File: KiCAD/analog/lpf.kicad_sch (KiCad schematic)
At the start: 74 parts, among them J16 Screw_Terminal_01x02, J25 Screw_Terminal_01x02, J26 Screw_Terminal_01x02, J27 Screw_Terminal_01x02, J28 Filter In, K1 Relay_RSS-SR042P, K2 Relay_RSS-SR042P, K3 Relay_RSS-SR042P, K4 Relay_RSS-SR042P, Q1 2N7000, Q3 2N7000, Q8 2N7000, Q9 2N7000, U2 LM7171xIN

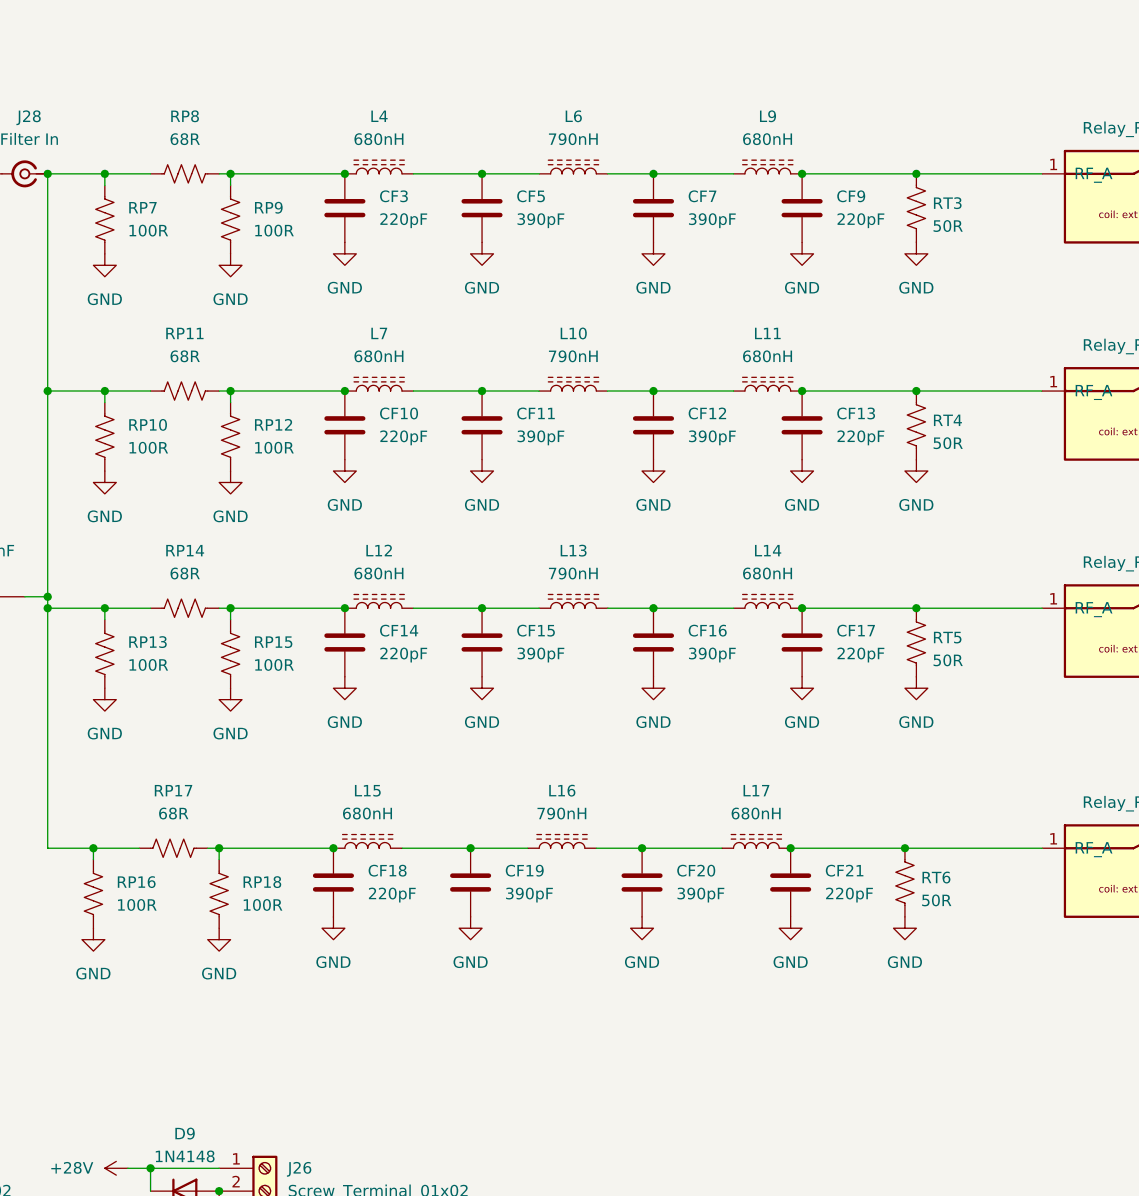
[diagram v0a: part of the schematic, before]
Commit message: KiCad revC: band-ID test points on each LPF input
Four test points added at the input node of each LPF (just after the
pi attenuator pad, at the junction with C1 shunt cap).  Reference
designators encode the band so that netlist/schematic consumers can
unambiguously identify which LPF cluster is for which band:

  TP20M  at 20 m LPF input
  TP17M  at 17 m LPF input
  TP15M  at 15 m LPF input
  TP10M  at 10 m LPF input

Dual-purpose: provides bench-probe access to the per-band LPF input
signal for debugging, and gives silkscreen labels on the PCB that make
the band assignment obvious at assembly time.

Co-Authored-By: Claude Opus 4.7 <noreply@anthropic.com>
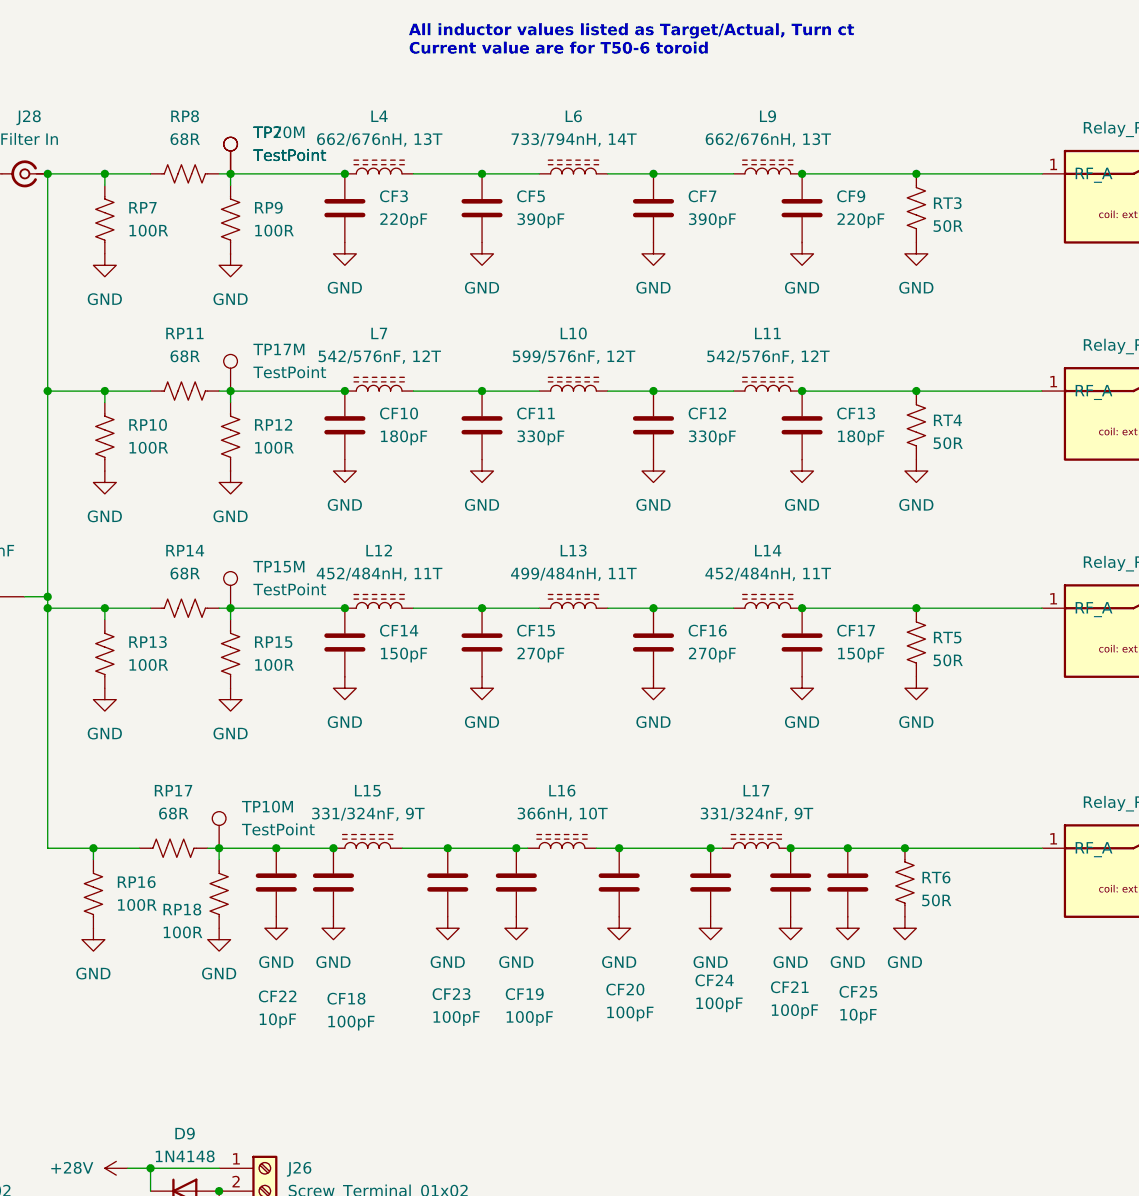
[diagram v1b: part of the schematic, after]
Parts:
- added CF22, CF25: 10pF, Capacitor_THT:C_Disc_D6.0mm_W2.5mm_P5.00mm, symbol Device:C
- added CF23, CF24: 100pF, Capacitor_THT:C_Disc_D6.0mm_W2.5mm_P5.00mm, symbol Device:C
- added TP10M, TP15M, TP17M, TP20M, TP7: TestPoint, symbol Connector:TestPoint
- CF10, CF13: value 220pF -> 180pF
- CF11, CF12: value 390pF -> 330pF
- CF14, CF17: value 220pF -> 150pF
- CF15, CF16: value 390pF -> 270pF
- CF18, CF21: value 220pF -> 100pF
- CF19, CF20: value 390pF -> 100pF
- L10: value 790nH -> 599/576nF, 12T
- L11, L7: value 680nH -> 542/576nF, 12T
- L12, L14: value 680nH -> 452/484nH, 11T
- L13: value 790nH -> 499/484nH, 11T
- L15, L17: value 680nH -> 331/324nF, 9T
- L16: value 790nH -> 366nH, 10T
- L4, L9: value 680nH -> 662/676nH, 13T
- L6: value 790nH -> 733/794nH, 14T
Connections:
- net GND: now also CF22.2, CF23.2, CF24.2, CF25.2
- net at CF18.1, L15.1, RP17.2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: now also CF22.1, TP10M.1
- net at CF19.1, L15.2, L16.1: now also CF23.1
- net at CF10.1, L7.1, RP11.2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: now also TP17M.1
- net at CF3.1, L4.1, RP8.2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: now also TP20M.1, TP7.1
- net at CF14.1, L12.1, RP14.2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: now also TP15M.1
- net at CF20.1, L16.2, L17.1: now also CF24.1
- net at CF21.1, K1.1 (RF_A), L17.2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: now also CF25.1
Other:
- note added: "All inductor values listed as Target/Actual, Turn ct Current value are for T50-6 toroid"
- moved on the sheet: CF19, CF20

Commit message: KiCad revC: 15 missing footprints assigned + T68->T50 inductor swap
Fifteen components across the LPF and DAC Control sheets had empty
Footprint fields.  Assigned appropriate footprints matching project
conventions already used by equivalent parts:

LPF sheet (12):
  C9 100nF  -> Capacitor_THT:C_Disc_D5.0mm_W2.5mm_P5.00mm
  C10 10nF -> Capacitor_THT:C_Disc_D6.0mm_W2.5mm_P5.00mm
  R11 1K   -> Resistor_THT:R_Axial_DIN0207_L6.3mm_D2.5mm_P10.16mm_Horizontal
  J16, J25, J26, J27 (relay coil screw terminals)
           -> TerminalBlock_Phoenix:TerminalBlock_Phoenix_MKDS-1,5-2_1x02_P5.00mm_Horizontal
  TP7, TP10M1, TP15M1, TP17M1, TP20M1 (test points)
           -> Connector_PinHeader_2.54mm:PinHeader_1x01_P2.54mm_Vertical

DAC Control sheet (3):
  R10 10K  -> same resistor footprint as above
  J11      -> same Phoenix screw-terminal footprint as above
  U4 MCP4922-EP -> Package_DIP:DIP-14_W7.62mm (PDIP, consistent with
                   the LM7171 PDIP-8 footprints already in use)

Also in this commit:
  - Nine inductor footprints swapped from T68-6 to T50-6 variants
    (L7, L10, L11, L12, L13, L14, L15, L16, L17 -- the 17m, 15m, 10m
    LPF inductors; L4, L6, L9 were already T50-6).  Correctly reflects
    that all four LPFs now use T50-6 cores.
  - Netlist regenerated by user to pick up the TP band-ID symbols
    (TP20M1, TP17M1, TP15M1, TP10M1) and the footprint changes.

Co-Authored-By: Claude Opus 4.7 <noreply@anthropic.com>
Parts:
- C10: footprint (none) -> Capacitor_THT:C_Disc_D6.0mm_W2.5mm_P5.00mm
- C9: footprint (none) -> Capacitor_THT:C_Disc_D5.0mm_W2.5mm_P5.00mm
- J16, J25, J26, J27: footprint (none) -> TerminalBlock_Phoenix:TerminalBlock_Phoenix_MKDS-1,5-2_1x02_P5.00mm_Horizontal
- L10: value 599/576nF, 12T -> 599/576nH, 12T; footprint xmitter:T68-6_Vertical_HandWound -> xmitter:T50-6_Vertical_HandWound
- L11: value 542/576nF, 12T -> 542/576nH 12T; footprint xmitter:T68-6_Flat_HandWound -> xmitter:T50-6_Flat_HandWound
- L12, L14, L15, L17: footprint xmitter:T68-6_Flat_HandWound -> xmitter:T50-6_Flat_HandWound
- L13: footprint xmitter:T68-6_Vertical_HandWound -> xmitter:T50-6_Vertical_HandWound
- L16: value 366nH, 10T -> 366/400nH, 10T; footprint xmitter:T68-6_Vertical_HandWound -> xmitter:T50-6_Vertical_HandWound
- L6: value 733/794nH, 14T -> 733/784nH, 14T
- L7: value 542/576nF, 12T -> 542/576nH, 12T; footprint xmitter:T68-6_Flat_HandWound -> xmitter:T50-6_Flat_HandWound
- R11: footprint (none) -> Resistor_THT:R_Axial_DIN0207_L6.3mm_D2.5mm_P10.16mm_Horizontal
- TP10M1: renamed from TP10M; footprint (none) -> Connector_PinHeader_2.54mm:PinHeader_1x01_P2.54mm_Vertical
- TP15M1: renamed from TP15M; footprint (none) -> Connector_PinHeader_2.54mm:PinHeader_1x01_P2.54mm_Vertical
- TP17M1: renamed from TP17M; footprint (none) -> Connector_PinHeader_2.54mm:PinHeader_1x01_P2.54mm_Vertical
- TP20M1: renamed from TP20M; footprint (none) -> Connector_PinHeader_2.54mm:PinHeader_1x01_P2.54mm_Vertical
- TP7: footprint (none) -> Connector_PinHeader_2.54mm:PinHeader_1x01_P2.54mm_Vertical
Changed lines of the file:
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@@
 			)
 		)
-		(property "Value" "542/576nF, 12T"
+		(property "Value" "542/576nH 12T"
 			(at 156.21 58.42 90)
 			(show_name no)
@@
 			)
 		)
-		(property "Footprint" "xmitter:T68-6_Flat_HandWound"
+		(property "Footprint" "xmitter:T50-6_Flat_HandWound"
 			(at 156.21 62.23 0)
 			(hide yes)
@@
 			)
 		)
-		(property "Footprint" ""
+		(property "Footprint" "TerminalBlock_Phoenix:TerminalBlock_Phoenix_MKDS-1,5-2_1x02_P5.00mm_Horizontal"
 			(at 49.53 175.26 0)
 			(hide yes)
@@
 			)
 		)
-		(property "Footprint" "xmitter:T68-6_Flat_HandWound"
+		(property "Footprint" "xmitter:T50-6_Flat_HandWound"
 			(at 111.76 113.03 0)
 			(hide yes)
@@
 		(dnp no)
 		(fields_autoplaced yes)
-		(property "Reference" "TP10M"
+		(property "Reference" "TP10M1"
 			(at 97.79 108.4579 0)
 			(show_name no)
@@
 			)
 		)
-		(property "Footprint" ""
+		(property "Footprint" "Connector_PinHeader_2.54mm:PinHeader_1x01_P2.54mm_Vertical"
 			(at 100.33 113.03 0)
 			(hide yes)
@@
 			(project "analog"
 				(path "/d3de40b8-856b-4fbd-829c-f45ffcd55742/9f79433a-f39c-4c2b-819d-3c5f5869f524"
-					(reference "TP10M")
+					(reference "TP10M1")
 					(unit 1)
 				)
@@
 			)
 		)
-		(property "Footprint" ""
+		(property "Footprint" "Connector_PinHeader_2.54mm:PinHeader_1x01_P2.54mm_Vertical"
 			(at 101.6 38.1 0)
 			(hide yes)
@@
 			)
 		)
-		(property "Value" "542/576nF, 12T"
+		(property "Value" "542/576nH, 12T"
 			(at 113.03 58.42 90)
 			(show_name no)
@@
 			)
 		)
-		(property "Footprint" "xmitter:T68-6_Flat_HandWound"
+		(property "Footprint" "xmitter:T50-6_Flat_HandWound"
 			(at 113.03 62.23 0)
 			(hide yes)
@@
 		(dnp no)
 		(fields_autoplaced yes)
-		(property "Reference" "TP17M"
+		(property "Reference" "TP17M1"
 			(at 99.06 57.6579 0)
 			(show_name no)
@@
 			)
 		)
-		(property "Footprint" ""
+		(property "Footprint" "Connector_PinHeader_2.54mm:PinHeader_1x01_P2.54mm_Vertical"
 			(at 101.6 62.23 0)
 			(hide yes)
@@
 			(project "analog"
 				(path "/d3de40b8-856b-4fbd-829c-f45ffcd55742/9f79433a-f39c-4c2b-819d-3c5f5869f524"
-					(reference "TP17M")
+					(reference "TP17M1")
 					(unit 1)
 				)
@@
 			)
 		)
-		(property "Footprint" ""
+		(property "Footprint" "Capacitor_THT:C_Disc_D6.0mm_W2.5mm_P5.00mm"
 			(at 35.56 81.5848 0)
 			(hide yes)
@@
 			)
 		)
-		(property "Value" "366nH, 10T"
+		(property "Value" "366/400nH, 10T"
 			(at 133.35 109.22 90)
 			(show_name no)
@@
 			)
 		)
-		(property "Footprint" "xmitter:T68-6_Vertical_HandWound"
+		(property "Footprint" "xmitter:T50-6_Vertical_HandWound"
 			(at 133.35 113.03 0)
 			(hide yes)
@@
 			)
 		)
-		(property "Footprint" ""
+		(property "Footprint" "TerminalBlock_Phoenix:TerminalBlock_Phoenix_MKDS-1,5-2_1x02_P5.00mm_Horizontal"
 			(at 100.33 176.53 0)
 			(hide yes)
@@
 		(dnp no)
 		(fields_autoplaced yes)
-		(property "Reference" "TP15M"
+		(property "Reference" "TP15M1"
 			(at 99.06 81.7879 0)
 			(show_name no)
@@
 			)
 		)
-		(property "Footprint" ""
+		(property "Footprint" "Connector_PinHeader_2.54mm:PinHeader_1x01_P2.54mm_Vertical"
 			(at 101.6 86.36 0)
 			(hide yes)
@@
 			(project "analog"
 				(path "/d3de40b8-856b-4fbd-829c-f45ffcd55742/9f79433a-f39c-4c2b-819d-3c5f5869f524"
-					(reference "TP15M")
+					(reference "TP15M1")
 					(unit 1)
 				)
@@
 			)
 		)
-		(property "Footprint" "xmitter:T68-6_Flat_HandWound"
+		(property "Footprint" "xmitter:T50-6_Flat_HandWound"
 			(at 113.03 86.36 0)
 			(hide yes)
@@
 			)
 		)
-		(property "Value" "733/794nH, 14T"
+		(property "Value" "733/784nH, 14T"
 			(at 134.62 34.29 90)
 			(show_name no)
@@
 			)
 		)
-		(property "Value" "599/576nF, 12T"
+		(property "Value" "599/576nH, 12T"
 			(at 134.62 58.42 90)
 			(show_name no)
@@
 			)
 		)
-		(property "Footprint" "xmitter:T68-6_Vertical_HandWound"
+		(property "Footprint" "xmitter:T50-6_Vertical_HandWound"
 			(at 134.62 62.23 0)
 			(hide yes)
@@
 			)
 		)
-		(property "Footprint" "xmitter:T68-6_Vertical_HandWound"
+		(property "Footprint" "xmitter:T50-6_Vertical_HandWound"
 			(at 134.62 86.36 0)
 			(hide yes)
@@
 			)
 		)
-		(property "Footprint" "xmitter:T68-6_Flat_HandWound"
+		(property "Footprint" "xmitter:T50-6_Flat_HandWound"
 			(at 154.94 113.03 0)
 			(hide yes)
@@
 			)
 		)
-		(property "Footprint" ""
+		(property "Footprint" "Capacitor_THT:C_Disc_D5.0mm_W2.5mm_P5.00mm"
 			(at 73.66 84.1248 0)
 			(hide yes)
@@
 		(dnp no)
 		(fields_autoplaced yes)
-		(property "Reference" "TP20M"
+		(property "Reference" "TP20M1"
 			(at 99.06 33.5279 0)
 			(show_name no)
@@
 			)
 		)
-		(property "Footprint" ""
+		(property "Footprint" "Connector_PinHeader_2.54mm:PinHeader_1x01_P2.54mm_Vertical"
 			(at 101.6 38.1 0)
 			(hide yes)
@@
 			(project "analog"
 				(path "/d3de40b8-856b-4fbd-829c-f45ffcd55742/9f79433a-f39c-4c2b-819d-3c5f5869f524"
-					(reference "TP20M")
+					(reference "TP20M1")
 					(unit 1)
 				)
@@
 			)
 		)
-		(property "Footprint" ""
+		(property "Footprint" "TerminalBlock_Phoenix:TerminalBlock_Phoenix_MKDS-1,5-2_1x02_P5.00mm_Horizontal"
 			(at 49.53 148.59 0)
 			(hide yes)
@@
 			)
 		)
-		(property "Footprint" ""
+		(property "Footprint" "TerminalBlock_Phoenix:TerminalBlock_Phoenix_MKDS-1,5-2_1x02_P5.00mm_Horizontal"
 			(at 100.33 148.59 0)
 			(hide yes)
@@
 			)
 		)
-		(property "Footprint" "xmitter:T68-6_Flat_HandWound"
+		(property "Footprint" "xmitter:T50-6_Flat_HandWound"
 			(at 156.21 86.36 0)
 			(hide yes)
@@
 			)
 		)
-		(property "Footprint" ""
+		(property "Footprint" "Resistor_THT:R_Axial_DIN0207_L6.3mm_D2.5mm_P10.16mm_Horizontal"
 			(at 36.576 86.614 90)
 			(hide yes)

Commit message: revD: analog board — DGFET+RC+buffer chain, LPF moved to ss_pa, PCB resized
Architecture change motivated by the Rev C sim finding that the LM7171
PP driver's +/-12V rails capped clean output at ~4.5W (see commit
3ce203d). Rev D delegates the gain-driver job to an external PA stage
(expected: QRP Labs 10W kit), so the analog board now just:
  Si5351 -> DGFET keyer -> R1(50)+C1(100p) RC @ 32MHz
         -> U1 LM7171 unity-gain follower -> R2(50) back-match -> J1 coax

Analog board changes (vfo_complete.kicad_sch):
  * DELETED: U10, U11, U12 (LM7171 PP driver chain) + feedback R/C,
    AC-coupling caps, V_BIAS network, R_GA/R_GB, C_GA/C_GB, J3/J4
    (dual-ended PP coax outputs)
  * DELETED: U2 reconstruction LPF stage (part of lpf.kicad_sch which
    is now emptied -- content moved to ss_pa/lpf.kicad_sch)
  * ADDED: R1=50R + C1=100pF (32 MHz single-pole RC snubber at the
    DGFET drain), U1 LM7171 unity-gain follower, R2=50R output
    back-match, J1 Conn_Coaxial_Small (new single-ended RF output),
    C2/C3=100nF op-amp bypass caps

Arduino sheet (arduino.kicad_sch):
  * ADDED: J2 Amphenol RJE1D-188 RJ45 for new external LPF board
    - Pins 1,2,3,6: RLY_10/15/17/20 band-select signals from PCF8575
    - Pins 5,8: GRID_CTL_A/B reserved spares for potential future
      tube PA (no other destination on the board, intentional)
    - Pins 4,7,SH: GND
  * ADDED: RLY_40 provision (not yet routed to J2, provision only)
  * T568B wire-pair arrangement for noise immunity

LPF content moved from analog/lpf.kicad_sch -> ss_pa/lpf.kicad_sch
(empty analog LPF sheet remains as a shell; delete later or repurpose).

PCB (analog.kicad_pcb):
  * Resized board outline from oversized 228x178 mm to 200x150 mm
    landscape (300 cm^2 / 46.5 in^2), centered on A3 at (210, 148.5)
  * Four M3 mounting holes H1-H4 placed 5 mm in from each corner
    (hole span 190 x 140 mm)
  * Added "board_only" attribute to each mounting hole so KiCad no
    longer flags them for deletion in Update PCB f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
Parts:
- removed C10: 10nF, Capacitor_THT:C_Disc_D6.0mm_W2.5mm_P5.00mm, symbol Device:C
- removed C9: 100nF, Capacitor_THT:C_Disc_D5.0mm_W2.5mm_P5.00mm, symbol Device:C
- removed C91, C96: 10uF, Capacitor_THT:CP_Radial_D5.0mm_P2.00mm, symbol Device:C_Polarized_US
- removed C93, C97: 100nF, Capacitor_THT:C_Disc_D5.0mm_W2.5mm_P5.00mm, symbol Device:C_US
- removed C94, C98: 10nF, Capacitor_THT:C_Disc_D6.0mm_W2.5mm_P5.00mm, symbol Device:C_US
- removed C95: 2pF, xmitter:C_Axial_Kemet_Aximax_C41X_L4.5mm_D2.6mm_P7.62mm_Horizontal, symbol Device:C_US
- removed CF10, CF13: 180pF, Capacitor_THT:C_Disc_D6.0mm_W2.5mm_P5.00mm, symbol Device:C
- removed CF11, CF12: 330pF, Capacitor_THT:C_Disc_D7.5mm_W2.5mm_P5.00mm, symbol Device:C
- removed CF14, CF17: 150pF, Capacitor_THT:C_Disc_D6.0mm_W2.5mm_P5.00mm, symbol Device:C
- removed CF15, CF16: 270pF, Capacitor_THT:C_Disc_D7.5mm_W2.5mm_P5.00mm, symbol Device:C
- removed CF18, CF21, CF23, CF24: 100pF, Capacitor_THT:C_Disc_D6.0mm_W2.5mm_P5.00mm, symbol Device:C
- removed CF19, CF20: 100pF, Capacitor_THT:C_Disc_D7.5mm_W2.5mm_P5.00mm, symbol Device:C
- removed CF22, CF25: 10pF, Capacitor_THT:C_Disc_D6.0mm_W2.5mm_P5.00mm, symbol Device:C
- removed CF3, CF9: 220pF, Capacitor_THT:C_Disc_D6.0mm_W2.5mm_P5.00mm, symbol Device:C
- removed CF5, CF7: 390pF, Capacitor_THT:C_Disc_D7.5mm_W2.5mm_P5.00mm, symbol Device:C
- removed D10, D7, D8, D9: 1N4148, Diode_THT:D_DO-35_SOD27_P7.62mm_Horizontal, symbol Diode:1N4148
- removed J16, J25, J26, J27: Screw_Terminal_01x02, TerminalBlock_Phoenix:TerminalBlock_Phoenix_MKDS-1,5-2_1x02_P5.00mm_Horizontal, symbol Connector:Screw_Terminal_01x02
- removed J28: Filter In, Connector_Coaxial:SMA_Amphenol_132134_Vertical, symbol Connector:Conn_Coaxial_Small
- removed K1, K2, K3, K4: Relay_RSS-SR042P, xmitter:Relay_SPST_RelComm_RSS-SR042P, symbol xmitter:Relay_SPST_RSS-SR042P
- removed L10: 599/576nH, 12T, xmitter:T50-6_Vertical_HandWound, symbol Device:L_Ferrite
- removed L11: 542/576nH 12T, xmitter:T50-6_Flat_HandWound, symbol Device:L_Ferrite
- removed L12, L14: 452/484nH, 11T, xmitter:T50-6_Flat_HandWound, symbol Device:L_Ferrite
- removed L13: 499/484nH, 11T, xmitter:T50-6_Vertical_HandWound, symbol Device:L_Ferrite
- removed L15, L17: 331/324nF, 9T, xmitter:T50-6_Flat_HandWound, symbol Device:L_Ferrite
- removed L16: 366/400nH, 10T, xmitter:T50-6_Vertical_HandWound, symbol Device:L_Ferrite
- removed L4, L9: 662/676nH, 13T, xmitter:T50-6_Vertical_HandWound, symbol Device:L_Ferrite
- removed L6: 733/784nH, 14T, xmitter:T50-6_Flat_HandWound, symbol Device:L_Ferrite
- removed L7: 542/576nH, 12T, xmitter:T50-6_Flat_HandWound, symbol Device:L_Ferrite
- removed Q1, Q3, Q8, Q9: 2N7000, Package_TO_SOT_THT:TO-92_Inline, symbol Transistor_FET:2N7000
- removed R11, R42: 1K, Resistor_THT:R_Axial_DIN0207_L6.3mm_D2.5mm_P10.16mm_Horizontal, symbol Device:R_US
- removed R43: 4.7K, Resistor_THT:R_Axial_DIN0207_L6.3mm_D2.5mm_P10.16mm_Horizontal, symbol Device:R_US
- removed RP10, RP12, RP13, RP15, RP16, RP18, RP7, RP9: 100R, Resistor_THT:R_Axial_DIN0207_L6.3mm_D2.5mm_P10.16mm_Horizontal, symbol Device:R_US
- removed RP11, RP14, RP17, RP8: 68R, Resistor_THT:R_Axial_DIN0207_L6.3mm_D2.5mm_P10.16mm_Horizontal, symbol Device:R_US
- removed RT3, RT4, RT5, RT6: 50R, Resistor_THT:R_Axial_DIN0207_L6.3mm_D2.5mm_P10.16mm_Horizontal, symbol Device:R_US
- removed TP10M1, TP15M1, TP17M1, TP20M1, TP7: TestPoint, Connector_PinHeader_2.54mm:PinHeader_1x01_P2.54mm_Vertical, symbol Connector:TestPoint
- removed U2: LM7171xIN, Package_DIP:DIP-8_W7.62mm, symbol Amplifier_Operational:LM7171xIN
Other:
- note removed: "All inductor values listed as Target/Actual, Turn ct Current value are for T50-6 toroid"
